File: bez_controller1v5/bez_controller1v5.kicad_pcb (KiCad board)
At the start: 4 copper layers, 100 x 60 mm, 80 parts, among them J1 Conn_01x03_Male, J10 Conn_01x07_Socket, J11 Conn_01x03_Male, J12 Conn_01x03_Male, J13 USB_B_Mini, J14 JTAG Conn_01x06_Male, J15 IMU Conn_01x08_Female, J2 Conn_01x03_Male, J3 Conn_01x03_Male, J4 Screw_Terminal_01x02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

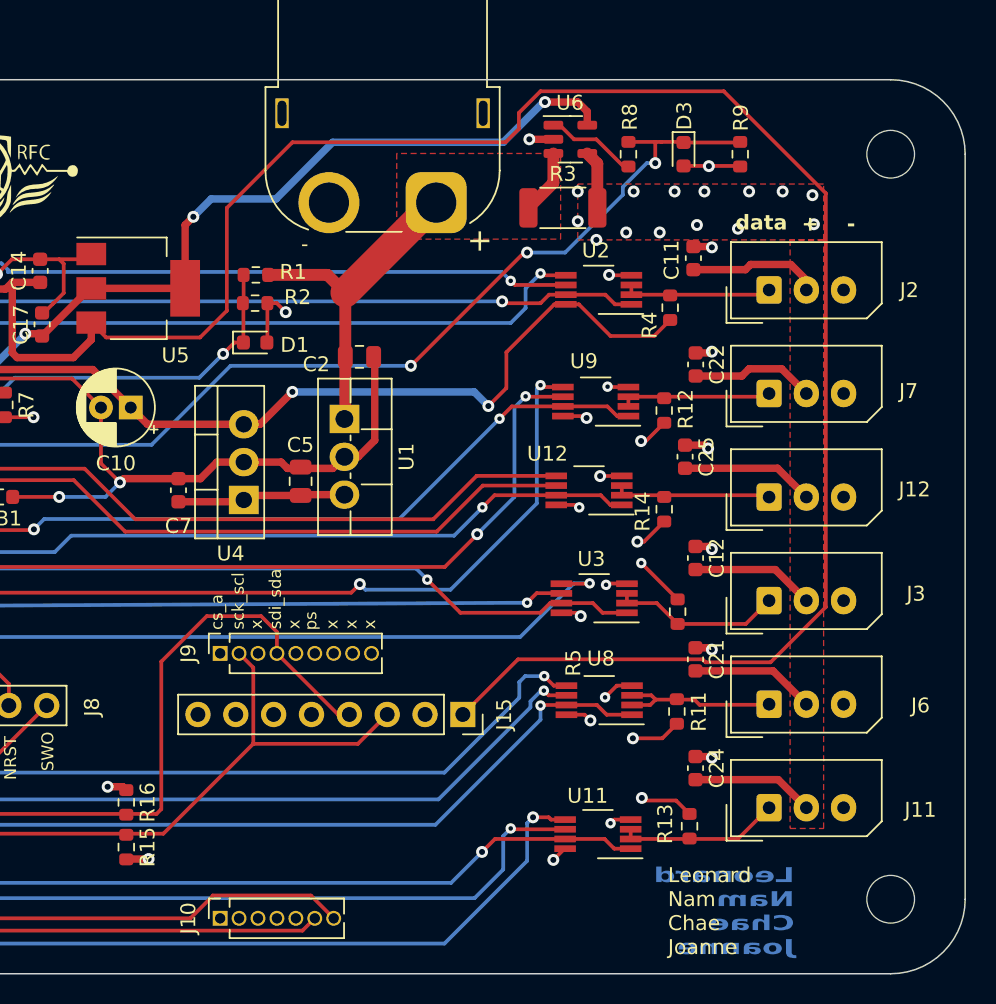
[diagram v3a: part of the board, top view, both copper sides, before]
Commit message: fix before manufacturing: move power trace away from 12V, added member names on silkscreen
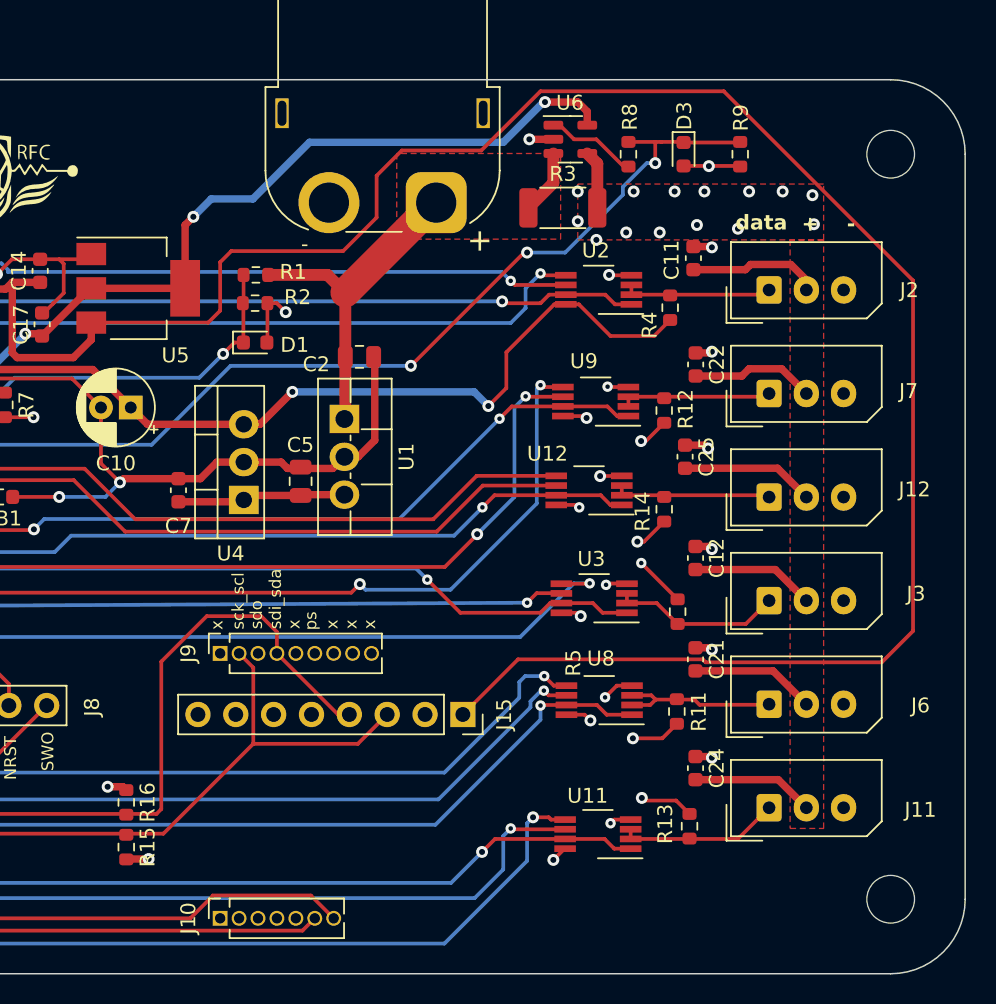
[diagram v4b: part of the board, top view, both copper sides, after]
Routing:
- net /power: track 146.2 -> 153.5 mm
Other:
- board text added: "Joanne"
- board text added: "Leonard Chae Nam"
- board text added: "sdo"
- board text removed: "Leonard Nam Chae Joanne"
- board text removed: "cs_a"
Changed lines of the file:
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@@
       (drillshape 0)
       (scaleselection 1)
-      (outputdirectory "Manufacturing/")
+      (outputdirectory "manufacturing/")
     )
   )
@@
   (gr_line (start 35 26) (end 125 26)
     (stroke (width 0.1) (type default)) (layer "Edge.Cuts"))
-  (gr_text "Leonard\nNam\nChae\nJoanne" (at 118.55 84.8) (layer "B.Cu")
-    (effects (font (size 1 1.5) (thickness 0.25) bold) (justify left bottom mirror))
-  )
   (gr_text "GPIO2" (at 44.4 83.275 90) (layer "F.SilkS")
     (effects (font (size 0.8 0.8) (thickness 0.15) bold) (justify left bottom))
@@
     (effects (font (size 1 1) (thickness 0.2) bold) (justify left bottom))
   )
-  (gr_text "x" (at 82.9 62.875 90) (layer "F.SilkS")
+  (gr_text "sdo" (at 82.9 62.875 90) (layer "F.SilkS")
     (effects (font (size 0.8 0.8) (thickness 0.15)) (justify left bottom))
   )
@@
     (effects (font (size 0.8 0.8) (thickness 0.15)) (justify left bottom))
   )
-  (gr_text "cs_a" (at 80.25 62.925 90) (layer "F.SilkS")
+  (gr_text "x" (at 80.25 62.925 90) (layer "F.SilkS")
     (effects (font (size 0.8 0.8) (thickness 0.15)) (justify left bottom))
   )
@@
     (effects (font (size 0.8 0.8) (thickness 0.15)) (justify left bottom))
   )
-  (gr_text "Leonard\nNam\nChae\nJoanne" (at 110.05 84.8) (layer "F.SilkS")
-    (effects (font (size 1 1) (thickness 0.15)) (justify left bottom))
-  )
   (gr_text "x" (at 87.975 62.875 90) (layer "F.SilkS")
     (effects (font (size 0.8 0.8) (thickness 0.15)) (justify left bottom))
@@
     (effects (font (size 0.8 0.8) (thickness 0.15)) (justify left bottom))
   )
+  (gr_text "Joanne" (at 111.75 85) (layer "Edge.Cuts")
+    (effects (font (size 1 1) (thickness 0.15)) (justify left bottom))
+  )
+  (gr_text "Leonard\nChae\nNam" (at 111.75 83.5) (layer "Edge.Cuts")
+    (effects (font (size 1 1) (thickness 0.15)) (justify left bottom))
+  )
   (dimension (type aligned) (layer "Dwgs.User")
     (pts (xy 30 81) (xy 130 81))
@@
   (segment (start 84.85 46.95) (end 97.05 46.95) (width 0.5) (layer "B.Cu") (net 5))
   (segment (start 97.05 46.95) (end 98 47.9) (width 0.5) (layer "B.Cu") (net 5))
+  (segment (start 80 41.5) (end 79.2 42.3) (width 0.25) (layer "F.Cu") (net 6))
   (segment (start 70.15 44.65) (end 71.35 43.45) (width 0.5) (layer "F.Cu") (net 6))
-  (segment (start 100.05 28.224695) (end 100.05 29.3) (width 0.25) (layer "F.Cu") (net 6))
-  (segment (start 80.45 41.5) (end 78.65 43.3) (width 0.25) (layer "F.Cu") (net 6))
+  (segment (start 99.99 64.9) (end 112.384052 64.9) (width 0.25) (layer "F.Cu") (net 6))
+  (segment (start 90.5 35.25) (end 88.25 37.5) (width 0.25) (layer "F.Cu") (net 6))
   (segment (start 65.5984 40.05) (end 66.0492 39.5992) (width 0.5) (layer "F.Cu") (net 6))
   (segment (start 71.35 43.45) (end 71.35 42.3) (width 0.5) (layer "F.Cu") (net 6))
-  (segment (start 112.577818 65.1) (end 116.936261 65.1) (width 0.25) (layer "F.Cu") (net 6))
+  (segment (start 79.2 42.3) (end 71.35 42.3) (width 0.25) (layer "F.Cu") (net 6))
   (segment (start 66.0492 39.5992) (end 67.9196 39.5992) (width 0.5) (layer "F.Cu") (net 6))
-  (segment (start 112.377818 64.9) (end 112.577818 65.1) (width 0.25) (layer "F.Cu") (net 6))
   (segment (start 66.0492 44.3242) (end 66.375 44.65) (width 0.5) (layer "F.Cu") (net 6))
   (segment (start 66.0492 39.5992) (end 66.0492 44.3242) (width 0.5) (layer "F.Cu") (net 6))
   (segment (start 66.375 44.65) (end 70.15 44.65) (width 0.5) (layer "F.Cu") (net 6))
+  (segment (start 92.191242 30.75) (end 90.5 32.441242) (width 0.25) (layer "F.Cu") (net 6))
+  (segment (start 124.4 65.1) (end 126.5 63) (width 0.25) (layer "F.Cu") (net 6))
   (segment (start 56.425 40.05) (end 65.5984 40.05) (width 0.5) (layer "F.Cu") (net 6))
-  (segment (start 99.15 30.2) (end 84.85 30.2) (width 0.25) (layer "F.Cu") (net 6))
-  (segment (start 120.65 61.386261) (end 120.65 33.624695) (width 0.25) (layer "F.Cu") (net 6))
-  (segment (start 78.65 43.3) (end 72.35 43.3) (width 0.25) (layer "F.Cu") (net 6))
-  (segment (start 84.85 30.2) (end 80.45 34.6) (width 0.25) (layer "F.Cu") (net 6))
-  (segment (start 113.800305 26.775) (end 101.499695 26.775) (width 0.25) (layer "F.Cu") (net 6))
+  (segment (start 88.25 37.5) (end 80.75 37.5) (width 0.25) (layer "F.Cu") (net 6))
+  (segment (start 126.5 63) (end 126.5 39.474695) (width 0.25) (layer "F.Cu") (net 6))
+  (segment (start 80 38.25) (end 80 41.5) (width 0.25) (layer "F.Cu") (net 6))
+  (segment (start 97.524695 30.75) (end 92.191242 30.75) (width 0.25) (layer "F.Cu") (net 6))
   (segment (start 96.29 68.6) (end 99.99 64.9) (width 0.25) (layer "F.Cu") (net 6))
-  (segment (start 116.936261 65.1) (end 120.65 61.386261) (width 0.25) (layer "F.Cu") (net 6))
-  (segment (start 80.45 34.6) (end 80.45 41.5) (width 0.25) (layer "F.Cu") (net 6))
+  (segment (start 101.499695 26.775) (end 97.524695 30.75) (width 0.25) (layer "F.Cu") (net 6))
+  (segment (start 112.384052 64.9) (end 112.584052 65.1) (width 0.25) (layer "F.Cu") (net 6))
   (segment (start 55.7276 40.7474) (end 56.425 40.05) (width 0.5) (layer "F.Cu") (net 6))
   (segment (start 55.7276 43.1292) (end 55.7276 40.7474) (width 0.5) (layer "F.Cu") (net 6))
-  (segment (start 72.35 43.3) (end 71.35 42.3) (width 0.25) (layer "F.Cu") (net 6))
-  (segment (start 120.65 33.624695) (end 113.800305 26.775) (width 0.25) (layer "F.Cu") (net 6))
-  (segment (start 99.99 64.9) (end 112.377818 64.9) (width 0.25) (layer "F.Cu") (net 6))
-  (segment (start 101.499695 26.775) (end 100.05 28.224695) (width 0.25) (layer "F.Cu") (net 6))
-  (segment (start 100.05 29.3) (end 99.15 30.2) (width 0.25) (layer "F.Cu") (net 6))
+  (segment (start 126.5 39.474695) (end 113.800305 26.775) (width 0.25) (layer "F.Cu") (net 6))
+  (segment (start 112.584052 65.1) (end 124.4 65.1) (width 0.25) (layer "F.Cu") (net 6))
+  (segment (start 113.800305 26.775) (end 101.499695 26.775) (width 0.25) (layer "F.Cu") (net 6))
+  (segment (start 90.5 32.441242) (end 90.5 35.25) (width 0.25) (layer "F.Cu") (net 6))
+  (segment (start 80.75 37.5) (end 80 38.25) (width 0.25) (layer "F.Cu") (net 6))
   (segment (start 41.315 58.0552) (end 40.0448 58.0552) (width 0.25) (layer "F.Cu") (net 7))
   (segment (start 39.9198 59.8802) (end 40.7924 59.8802) (width 0.25) (layer "F.Cu") (net 7))
@@
   (segment (start 62.375 48.175) (end 62.375 47.625) (width 0.5) (layer "B.Cu") (net 7))
   (segment (start 62.375 47.625) (end 66.925 43.075) (width 0.5) (layer "B.Cu") (net 7))
-  (segment (start 79.4 34) (end 83.75 34) (width 0.5) (layer "B.Cu") (net 7))
-  (segment (start 66.925 43.075) (end 66.925 43.05) (width 0.5) (layer "B.Cu") (net 7))
-  (segment (start 99 30.2) (end 101.7 27.5) (width 0.5) (layer "B.Cu") (net 7))
-  (segment (start 83.75 34) (end 87.55 30.2) (width 0.5) (layer "B.Cu") (net 7))
   (segment (start 101.7 27.5) (end 101.8 27.5) (width 0.5) (layer "B.Cu") (net 7))
-  (segment (start 87.55 30.2) (end 99 30.2) (width 0.5) (layer "B.Cu") (net 7))
   (segment (start 78.2 35.2) (end 79.4 34) (width 0.5) (layer "B.Cu") (net 7))
+  (segment (start 82.2 34) (end 86 30.2) (width 0.5) (layer "B.Cu") (net 7))
+  (segment (start 66.925 43.075) (end 66.925 43.05) (width 0.5) (layer "B.Cu") (net 7))
+  (segment (start 99 30.2) (end 101.7 27.5) (width 0.5) (layer "B.Cu") (net 7))
+  (segment (start 79.4 34) (end 82.2 34) (width 0.5) (layer "B.Cu") (net 7))
+  (segment (start 86 30.2) (end 99 30.2) (width 0.5) (layer "B.Cu") (net 7))
   (segment (start 50 62.075) (end 52.2198 62.075) (width 0.25) (layer "F.Cu") (net 8))
   (segment (start 53.475 64.9) (end 53.475 63.365) (width 0.25) (layer "F.Cu") (net 8))

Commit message: ordered PCB
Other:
- board text added: "Leonard Chae Nam Joanne"
- board text removed: "Joanne"
- board text removed: "Leonard Chae Nam"
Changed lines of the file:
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@@
     (effects (font (size 0.8 0.8) (thickness 0.15)) (justify left bottom))
+  )
+  (gr_text "Leonard \nChae\nNam\nJoanne" (at 112.65 84.8) (layer "F.SilkS")
+    (effects (font (size 1 1) (thickness 0.15)) (justify left bottom))
   )
   (gr_text "3.3V" (at 54.5 82.375 90) (layer "F.SilkS")
@@
     (effects (font (size 0.8 0.8) (thickness 0.15)) (justify left bottom))
   )
-  (gr_text "Joanne" (at 111.75 85) (layer "Edge.Cuts")
-    (effects (font (size 1 1) (thickness 0.15)) (justify left bottom))
-  )
-  (gr_text "Leonard\nChae\nNam" (at 111.75 83.5) (layer "Edge.Cuts")
-    (effects (font (size 1 1) (thickness 0.15)) (justify left bottom))
-  )
   (dimension (type aligned) (layer "Dwgs.User")

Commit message: First iteration of the new board with new functions
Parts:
- removed G***: LOGO, LOGO
- added D10: BZV55B5V1, Diode_SMD:D_MiniMELF, B.Cu at (181.4, 54.5)
- added D5: BZV55B5V1, Diode_SMD:D_MiniMELF, B.Cu at (166.9, 54.5)
- added D6: BZV55B5V1, Diode_SMD:D_MiniMELF, B.Cu at (123.3, 54.5)
- added D7: BZV55B5V1, Diode_SMD:D_MiniMELF, B.Cu at (195.9, 54.5)
- added D8: BZV55B5V1, Diode_SMD:D_MiniMELF, B.Cu at (137.8, 54.5)
- added D9: BZV55B5V1, Diode_SMD:D_MiniMELF, B.Cu at (152.3, 54.5)
- added J16: MOLEX_Conn_Button, KiCad:CON_530480210_MOL, F.Cu at (170.5, 101.8)
- added J17: MOLEX_Conn_Button, KiCad:CON_530480210_MOL, F.Cu at (179.8, 101.8)
- added R17: 1k, Resistor_SMD:R_0603_1608Metric, F.Cu at (175.8, 102.0)
- C10: footprint Capacitor_THT:CP_Radial_D5.0mm_P2.00mm -> Capacitor_SMD:C_0603_1608Metric
- J11, J12, J2, J3, J6, J7: footprint Connector_Molex:Molex_SPOX_5267-03A_1x03_P2.50mm_Vertical -> KiCad:CONN_S3B-XH-ALFSN_JST
- J13: footprint USB-Library:USB_MINI -> KiCad:USB_MINI
- J14: value JTAG Conn_01x06_Male -> PPTC041LGBN-RC; footprint Connector_PinHeader_2.54mm:PinHeader_1x06_P2.54mm_Vertical -> KiCad:CONN_PPTC041LGBN-RC_SUL
- J15: value IMU Conn_01x08_Female -> Conn_01x03_Male; footprint Connector_PinSocket_2.54mm:PinSocket_1x08_P2.54mm_Vertical -> Connector_PinHeader_2.54mm:PinHeader_1x03_P2.54mm_Vertical
- R3: value 5m -> 10m
- R9: value 10k -> 1k
- U11, U12, U2, U3, U8, U9: footprint Package_SO:VSSOP-8_3.0x3.0mm_P0.65mm -> KiCad:VSSOP-8_3.0x3.0mm_P0.65mm
- moved H2 170.2 mm to (203.8, 53.0)
- moved D4 120.8 mm to (152.9, 73.3), turned to 180 degrees
- moved R2 119.2 mm to (196.9, 74.0)
- moved D1 119.0 mm to (196.9, 76.1)
- moved R1 118.2 mm to (196.1, 71.3), turned to -90 degrees
- moved R10 116.9 mm to (149.7, 73.3), turned to 180 degrees
- moved J4 116.6 mm to (203.9, 74.5), turned to -90 degrees
- moved C8 116.0 mm to (150.4, 88.2), turned to -90 degrees
- moved C6 107.6 mm to (141.6, 88.8), turned to 180 degrees
- moved FB1 106.4 mm to (170.8, 67.7), turned to -90 degrees
- moved J1 105.1 mm to (140.8, 69.0), turned to 90 degrees
- moved C16 104.6 mm to (148.0, 89.0), turned to 0 degrees
- moved R6 103.5 mm to (142.1, 72.7), turned to -90 degrees
- moved H4 103.4 mm to (203.8, 98.0)
- moved U7 102.0 mm to (145.3, 81.2), turned to 0 degrees
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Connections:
- C11 pad 2: +12V -> /post_shunt_12v
- C12 pad 2: +12V -> /post_shunt_12v
- C2 pad 1: +12V -> /post_shunt_12v
- C21 pad 2: +12V -> /post_shunt_12v
- C22 pad 2: +12V -> /post_shunt_12v
- C24 pad 2: +12V -> /post_shunt_12v
- C25 pad 2: +12V -> /post_shunt_12v
- J11 pad 2: +12V -> /post_shunt_12v
- J12 pad 2: +12V -> /post_shunt_12v
- J14 pad 1: +3.3V -> GND
- J14 pad 2: GND -> +3.3V
- J14 pad 3: GND -> /Screen_SCL
- J14 pad 4: /GPIO1 -> /Screen_SDA
- J15 pad 1: /power -> /SWO
- J15 pad 2: GND -> /SWO_or_Screen_SDA
- J15 pad 3: /SCK_SCL -> /Screen_SDA
- J2 pad 2: +12V -> /post_shunt_12v
- J3 pad 2: +12V -> /post_shunt_12v
- J6 pad 2: +12V -> /post_shunt_12v
- J7 pad 2: +12V -> /post_shunt_12v
- R3 pad 2: +12V -> /post_shunt_12v
- R9 pad 1: /V_shunt_read -> +3.3V
- R9 pad 2: GND -> /GPIO1
- U1 pad 1: +12V -> /post_shunt_12v
- U6 pad 4: +12V -> /post_shunt_12v
- U7 pad 10: /V_shunt_read -> unconnected-(U7-PC2-Pad10)
- U7 pad 2: /GPIO3 -> unconnected-(U7-PC13-Pad2)
- U7 pad 23: unconnected-(U7-PA7-Pad23) -> /V_shunt_read
- U7 pad 26: unconnected-(U7-PB0-Pad26) -> /V_bat_read
- U7 pad 29: /USART3_TX -> /Screen_SCL
- U7 pad 51: /INT1 -> /USART3_TX
- U7 pad 52: /INT2 -> unconnected-(U7-PC11-Pad52)
- U7 pad 55: /SWO -> /SWO_or_Screen_SDA
- U7 pad 8: unconnected-(U7-PC0-Pad8) -> /INT1
- U7 pad 9: /V_bat_read -> /INT2
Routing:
- net +3.3V: track 90.1 -> 283.7 mm, vias 13 -> 0
- net /power: track 153.5 -> 12.3 mm
- net +12V: track 82.2 -> 0.00 mm, vias 14 -> 0
- net /USART6_TX: track 126.1 -> 48.4 mm
- net /USART6_RX: track 117.2 -> 48.2 mm
- net /USART6_DIR: track 113.7 -> 48.0 mm
- net /INT1: track 90.2 -> 25.9 mm, vias 0 -> 1
- net /Screen_SCL: track 0.00 -> 61.3 mm, vias 0 -> 1
- net /INT2: track 88.5 -> 27.8 mm, vias 0 -> 1
- net /USART5_DIR: track 94.3 -> 34.9 mm
- net /SCK_SCL: track 94.2 -> 35.5 mm, vias 0 -> 1
- net /USB_D-: track 7.65 -> 64.9 mm, vias 0 -> 2
- net /USB_D+: track 7.64 -> 63.4 mm, vias 0 -> 2
- net /GPIO2: track 20.3 -> 73.9 mm
- net /SDI_SDA: track 92.3 -> 39.2 mm, vias 0 -> 1
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- added copper zone on F.Cu, net /post_shunt_12v
- added copper zone on B.Cu, net GND
- removed copper zone on In1.Cu, net +12V
- removed copper zone on In1.Cu, net +3.3V
- removed copper zone on In2.Cu, net GND
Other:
- board size 100 x 60 mm -> 130 x 65 mm
- board text removed: "+"
- board text removed: "-"
- board text removed: "3.3V"
- board text removed: "5V"
- board text removed: "GND"
- board text removed: "GPIO1"
- board text removed: "GPIO2"
- board text removed: "GPIO3"
- board text removed: "Leonard Chae Nam Joanne"
- board text removed: "NRST"
- board text removed: "SWO"
- board text removed: "TCK"
- board text removed: "TMS"
- board text removed: "USB_5V"
- board text removed: "data"
- board text removed: "ps"
- board text removed: "sck_scl"
- board text removed: "sdi_sda"
- board text removed: "sdo"
- board text removed: "x"

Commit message: Very rough changes for size constraint.
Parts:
- moved J14 72.1 mm to (176.2, 91.0)
- moved J8 51.7 mm to (184.8, 87.0)
- moved J15 50.0 mm to (167.8, 87.0), turned to 0 degrees
- moved R9 31.4 mm to (197.8, 97.7), turned to 180 degrees
- moved J16 28.2 mm to (197.6, 93.8), turned to 90 degrees
- moved R17 25.7 mm to (197.8, 88.5), turned to 180 degrees
- moved J17 24.7 mm to (197.5, 84.6), turned to 90 degrees
- moved R3 8.38 mm to (183.6, 68.3)
- moved D1 8.38 mm to (188.5, 76.7)
- moved D3 8.38 mm to (184.7, 79.1)
- moved J4 8.38 mm to (195.6, 75.1)
- moved R1 8.38 mm to (187.7, 71.9)
- moved R2 8.38 mm to (188.6, 74.7)
- moved R8 8.38 mm to (184.7, 75.7)
- moved U6 8.38 mm to (183.6, 72.0)
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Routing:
- net /GPIO1: track 60.0 -> 87.4 mm
- net /NRST: track 29.6 -> 55.2 mm
- net +3.3V: track 283.7 -> 306.3 mm
- net /TMS: track 52.5 -> 31.3 mm
- net /Screen_SCL: track 61.3 -> 42.5 mm
- net /TCK: track 56.2 -> 41.0 mm
- net /GPIO2: track 73.9 -> 88.8 mm
- net /SWO_or_Screen_SDA: track 45.5 -> 32.7 mm
- net /Screen_SDA: track 4.35 -> 16.9 mm
- net /V_bat_read: track 69.1 -> 60.5 mm
- net /V_shunt_read: track 67.5 -> 59.3 mm
- net /SWO: track 11.5 -> 4.38 mm
- net /USB_D+: track 63.4 -> 58.0 mm
- net +5V: track 88.2 -> 84.2 mm
- net /USB_D-: track 64.9 -> 61.4 mm
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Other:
- board size 130 x 65 mm -> 110 x 65 mm
- board text added: "Bez2 PCB Chae Arshiya Mike"
